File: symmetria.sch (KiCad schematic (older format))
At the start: 20 parts

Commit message: Complete Schematics and PCB footprinting
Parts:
- removed J?: USB_C_Receptacle_USB2.0, symbol Connector:USB_C_Receptacle_USB2.0
- added D1, D10, D11, D12, D13, D14, D15, D16, D17, D18, D19, D2, D20, D21, D22, D23, D24, D25, D26, D27, D28, D29, D3, D30, D31, D32, D33, D34, D35, D36, D37, D38, D39, D4, D5, D6, D7, D8, D9: D_Small, Diode_SMD:D_SOD-123, symbol Device:D_Small
- added MX1, MX10, MX11, MX12, MX13, MX14, MX15, MX16, MX17, MX18, MX19, MX2, MX20, MX21, MX22, MX23, MX24, MX25, MX26, MX27, MX28, MX29, MX3, MX30, MX31, MX32, MX33, MX34, MX35, MX36, MX4, MX5, MX6, MX7, MX8, MX9: MX-NoLED, MX_Only:MXOnly-1U-NoLED, symbol MX_Alps_Hybrid:MX-NoLED
- added MX37, MX39: MX-NoLED, MX_Only:MXOnly-1.5U-NoLED, symbol MX_Alps_Hybrid:MX-NoLED
- added MX38: MX-NoLED, MX_Only:MXOnly-7U-ReversedStabilizers-NoLED, symbol MX_Alps_Hybrid:MX-NoLED
- C1, C2, C3, C4, C5, C6, C7: renamed from C?; footprint (none) -> Capacitor_SMD:C_0805_2012Metric
- F1: renamed from F?; footprint (none) -> Fuse:Fuse_1206_3216Metric
- J2: renamed from J?; footprint (none) -> Type-C:USB_C_GCT_USB4085
- R1, R2, R3, R4, R5, R6: renamed from R?; footprint (none) -> Resistor_SMD:R_0805_2012Metric
- SW1: renamed from SW?; footprint (none) -> random-keyboard-parts:SKQG-1155865
- Y1: renamed from Y?; footprint (none) -> Crystal:Crystal_SMD_3225-4Pin_3.2x2.5mm
- gave numbers to parts that had none: 2
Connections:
- new net: D1.2 (A), MX1.2 (ROW)
- new net: D2.2 (A), MX2.2 (ROW)
- new net: D4.2 (A), MX4.2 (ROW)
- new net: D5.2 (A), MX5.2 (ROW)
- new net: D6.2 (A), MX6.2 (ROW)
- new net: D7.2 (A), MX7.2 (ROW)
- new net: D8.2 (A), MX8.2 (ROW)
- new net: D9.2 (A), MX9.2 (ROW)
- new net: D10.2 (A), MX10.2 (ROW)
- new net: D11.2 (A), MX11.2 (ROW)
- new net: D12.2 (A), MX12.2 (ROW)
- new net: D3.2 (A), MX3.2 (ROW)
- new net: D13.2 (A), MX13.2 (ROW)
- new net: D14.2 (A), MX14.2 (ROW)
- new net: D15.2 (A), MX15.2 (ROW)
- new net: D16.2 (A), MX16.2 (ROW)
- new net: D17.2 (A), MX17.2 (ROW)
- new net: D18.2 (A), MX18.2 (ROW)
- new net: D19.2 (A), MX19.2 (ROW)
- new net: D20.2 (A), MX20.2 (ROW)
- new net: D21.2 (A), MX21.2 (ROW)
- new net: D22.2 (A), MX22.2 (ROW)
- new net: D23.2 (A), MX23.2 (ROW)
- new net: D24.2 (A), MX24.2 (ROW)
- new net: D25.2 (A), MX25.2 (ROW)
- new net: D26.2 (A), MX26.2 (ROW)
- new net: D27.2 (A), MX27.2 (ROW)
- new net: D28.2 (A), MX28.2 (ROW)
- new net: D29.2 (A), MX29.2 (ROW)
- new net: D30.2 (A), MX30.2 (ROW)
- new net: D31.2 (A), MX31.2 (ROW)
- new net: D32.2 (A), MX32.2 (ROW)
- new net: D33.2 (A), MX33.2 (ROW)
- new net: D34.2 (A), MX34.2 (ROW)
- new net: D35.2 (A), MX35.2 (ROW)
- new net: D36.2 (A), MX36.2 (ROW)
- new net: D38.2 (A), MX38.2 (ROW)
- new net: D37.2 (A), MX37.2 (ROW)
- new net: D39.2 (A), MX39.2 (ROW)
- new net COL0: MX1.1 (COL), MX13.1 (COL), MX25.1 (COL)
- new net COL1: MX14.1 (COL), MX2.1 (COL), MX26.1 (COL), MX37.1 (COL)
- new net COL10: MX11.1 (COL), MX23.1 (COL), MX35.1 (COL), MX39.1 (COL)
- new net COL11: MX12.1 (COL), MX24.1 (COL), MX36.1 (COL)
- new net COL2: MX15.1 (COL), MX27.1 (COL), MX3.1 (COL)
- new net COL3: MX16.1 (COL), MX28.1 (COL), MX4.1 (COL)
- new net COL4: MX17.1 (COL), MX29.1 (COL), MX5.1 (COL)
- new net COL5: MX18.1 (COL), MX30.1 (COL), MX6.1 (COL)
- new net COL6: MX19.1 (COL), MX31.1 (COL), MX38.1 (COL), MX7.1 (COL)
- new net COL7: MX20.1 (COL), MX32.1 (COL), MX8.1 (COL)
- new net COL8: MX21.1 (COL), MX33.1 (COL), MX9.1 (COL)
- new net COL9: MX10.1 (COL), MX22.1 (COL), MX34.1 (COL)
- new net ROW0: D1.1 (K), D10.1 (K), D11.1 (K), D12.1 (K), D2.1 (K), D3.1 (K), D4.1 (K), D5.1 (K), D6.1 (K), D7.1 (K), D8.1 (K), D9.1 (K)
- new net ROW1: D13.1 (K), D14.1 (K), D15.1 (K), D16.1 (K), D17.1 (K), D18.1 (K), D19.1 (K), D20.1 (K), D21.1 (K), D22.1 (K), D23.1 (K), D24.1 (K)
- new net ROW2: D25.1 (K), D26.1 (K), D27.1 (K), D28.1 (K), D29.1 (K), D30.1 (K), D31.1 (K), D32.1 (K), D33.1 (K), D34.1 (K), D35.1 (K), D36.1 (K)
- new net ROW4: D37.1 (K), D38.1 (K), D39.1 (K)

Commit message: PCB Laid out
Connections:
- net COL0: now also U2.25 (PD4)
- net COL1: now also U2.26 (PD6)
- net COL10: now also U2.38 (PF5)
- net COL11: now also U2.39 (PF4)
- net COL2: now also U2.27 (PD7)
- net COL3: now also U2.28 (PB4)
- net COL4: now also U2.29 (PB5)
- net COL5: now also U2.30 (PB6)
- net COL6: now also U2.31 (PC6)
- net COL7: now also U2.32 (PC7)
- net COL8: now also U2.36 (PF7)
- net COL9: now also U2.37 (PF6)
- net ROW0: now also U2.22 (PD5)
- net ROW1: now also U2.21 (PD3)
- net ROW2: now also U2.20 (PD2)
- net ROW3: now reaches U2.19 (PD1)
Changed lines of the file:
@@
 Wire Wire Line
 	8150 1200 8650 1200
+Text GLabel 6050 4200 2    50   Input ~ 0
+ROW0
+Text GLabel 6050 4000 2    50   Input ~ 0
+ROW1
+Text GLabel 6050 3900 2    50   Input ~ 0
+ROW2
+Text GLabel 6050 3800 2    50   Input ~ 0
+ROW3
+Text GLabel 6050 5100 2    50   Input ~ 0
+COL11
+Text GLabel 6050 5200 2    50   Input ~ 0
+COL10
+Text GLabel 6050 5300 2    50   Input ~ 0
+COL9
+Text GLabel 6050 5400 2    50   Input ~ 0
+COL8
+Text GLabel 6050 3500 2    50   Input ~ 0
+COL7
+Text GLabel 6050 3400 2    50   Input ~ 0
+COL6
+Text GLabel 6050 3100 2    50   Input ~ 0
+COL5
+Text GLabel 6050 3000 2    50   Input ~ 0
+COL4
+Text GLabel 6050 2900 2    50   Input ~ 0
+COL3
+Text GLabel 6050 4400 2    50   Input ~ 0
+COL2
+Text GLabel 6050 4300 2    50   Input ~ 0
+COL1
+Text GLabel 6050 4100 2    50   Input ~ 0
+COL0
 $EndSCHEMATC

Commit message: Switch Tracing Complete
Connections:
- net ROW4 is gone; now on net ROW3: D37.1 (K), D38.1 (K), D39.1 (K)
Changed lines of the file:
@@
 ROW2
 Text GLabel 13100 6400 0    50   Input ~ 0
-ROW4
+ROW3
 Wire Wire Line
 	13100 6400 13650 6400

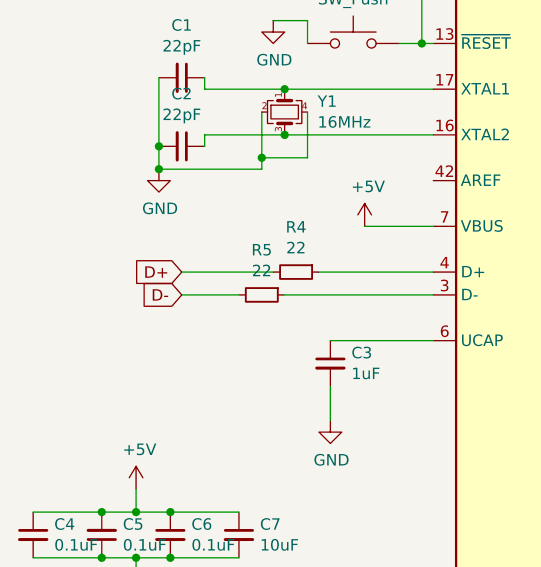
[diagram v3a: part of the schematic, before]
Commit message: PCB routing Finished
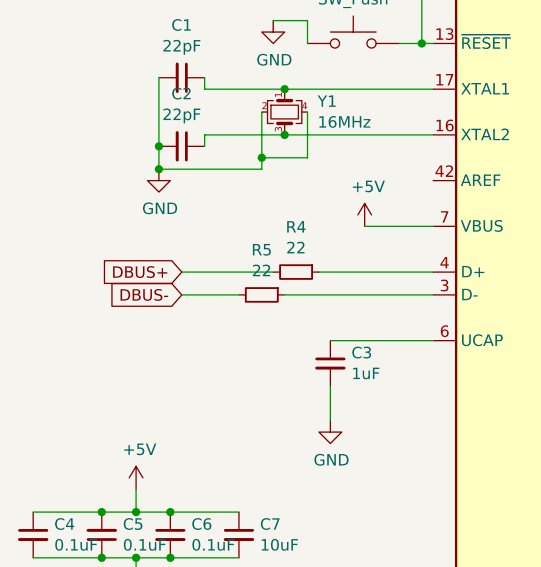
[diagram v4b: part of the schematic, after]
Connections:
- net D+ is gone; now on net DBUS+: R4.2
- net D- is gone; now on net DBUS-: R5.2
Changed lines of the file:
@@
 Connection ~ 3650 3050
 Text GLabel 3750 3500 0    50   Input ~ 0
-D+
+DBUS+
 Text GLabel 3750 3600 0    50   Input ~ 0
-D-
+DBUS-
 $Comp
 L power:GND #PWR0111
